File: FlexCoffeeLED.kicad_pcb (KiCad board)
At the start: 2 copper layers, 12.7 x 97.3 mm, 32 parts, among them IC1 NCP718ASN330T1G, IC2 PIC18F25K80-I_SO, IC3 MCP9904T-AE_9Q, J1 Conn_01x05_Male, J2 Conn_01x01_Male, J3 Conn_01x01_Male, Q1 2N3904, Q2 2N3904, Q3 2N3904, U1 PCA9306

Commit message: A Brand New Design
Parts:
- removed Q1, Q2, Q3: 2N3904, BillysCustomLibs:TO-92_Inline_Narrow_Oval_SMD
- removed R5: 450k, Resistors_SMD:R_0603
- removed R6: 200k, Resistors_SMD:R_0603
- removed R7, R8: 1k, Resistors_SMD:R_0603
- removed U1: PCA9306, SamacSys_Parts:SOP50P310X90-8N
- added C11: 0.1uF, Capacitors_SMD:C_0603, F.Cu at (195.6, 103.9)
- added IC4: LM75BDP,118, SamacSys_Parts:SOP65P490X110-8N, F.Cu at (187.6, 74.2)
- added LED4: WS2812B, LEDs:LED_WS2812B-PLCC4, F.Cu at (181.2, 57.9)
- added LED5: WS2812B, LEDs:LED_WS2812B-PLCC4, F.Cu at (181.2, 46.1)
- added LED6: WS2812B, LEDs:LED_WS2812B-PLCC4, F.Cu at (181.2, 34.3)
- C1, C4: value 1uF -> 15pF
- C7: value 2.2nF -> 15pF
- C8: value 2.2nF -> 0.1uF
- IC1: value NCP718ASN330T1G -> LM75BDP,118; footprint SamacSys_Parts:SOT95P280X100-5N -> SamacSys_Parts:SOP65P490X110-8N
- IC2: value PIC18F25K80-I_SO -> PIC16F18426-I_ST; footprint SamacSys_Parts:SOIC127P1030X265-28N -> SOP65P640X120-14N
- IC3: value MCP9904T-AE_9Q -> LM75BDP,118; footprint SamacSys_Parts:SON50P300X300X90-11N-D -> SamacSys_Parts:SOP65P490X110-8N
- J1: footprint BillysCustomLibs:Pin_Header_Straight_1x05_Pitch2.54mm_SMD_Flat -> Pin_Headers:Pin_Header_Straight_1x05_Pitch2.54mm
- J2, J3: value Conn_01x01_Male -> Conn_01x03_Male; footprint Pin_Headers:Pin_Header_Straight_1x01_Pitch2.54mm -> Pin_Headers:Pin_Header_Straight_1x03_Pitch2.54mm
- moved C7 66.2 mm to (173.5, 32.2), turned to 0 degrees
- moved JP1 64.3 mm to (168.1, 102.7)
- moved C2 64.2 mm to (170.4, 105.2)
- moved R2 64.2 mm to (168.7, 105.2)
- moved R1 63.6 mm to (168.7, 99.9)
- moved C8 61.8 mm to (196.9, 38.2), turned to 0 degrees
- moved IC3 60.5 mm to (187.7, 33.8)
- moved R3 56.3 mm to (195.7, 34.2)
- moved IC2 45.4 mm to (181.2, 97.7), turned to 270 degrees
- moved LED3 39.8 mm to (181.2, 69.7)
- moved C9 35.3 mm to (172.8, 101.4)
- moved C4 30.3 mm to (180.1, 70.9), turned to 180 degrees
- moved C6 22.5 mm to (180.5, 56.8), turned to 0 degrees
- moved C5 21.9 mm to (174.9, 93.8)
- moved C1 21.4 mm to (180.4, 86.5), turned to 180 degrees
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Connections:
- net Net-(IC2-Pad5) renamed /SCL2
- net Net-(IC2-Pad6) renamed /SDA2
- C1 pad 1: +5V -> /LED3
- C10 pad 1: /VREF2 -> +5V
- C2 pad 2: GND -> Net-(C2-Pad2)
- C3 pad 1: /LED1 -> /DIN
- C4 pad 1: +3V3 -> /LED4
- C6 pad 1: /LED3 -> /LED5
- C7 pad 1: /DP2 -> /LED6
- C7 pad 2: /DN2 -> GND
- C8 pad 1: /DP1 -> +5V
- C8 pad 2: /DN1 -> GND
- IC1 pad 1: +5V -> SDA_5V
- IC1 pad 2: GND -> SCL_5V
- IC1 pad 3: +5V -> Net-(IC1-Pad3)
- IC1 pad 5: +3V3 -> +5V
- IC2 pad 1: /MCLR -> +5V
- IC2 pad 10: Net-(IC2-Pad10) -> SCL_5V
- IC2 pad 11: Net-(IC2-Pad11) -> /DIN
- IC2 pad 12: Net-(IC2-Pad12) -> /PGC
- IC2 pad 13: Net-(IC2-Pad13) -> /PGD
- IC2 pad 14: SCL_5V -> GND
- IC2 pad 4: Net-(IC2-Pad4) -> /MCLR
- IC2 pad 8: GND -> Net-(IC2-Pad8)
- IC2 pad 9: Net-(IC2-Pad9) -> SDA_5V
- IC3 pad 1: +3V3 -> SDA_5V
- IC3 pad 2: /DP1 -> SCL_5V
- IC3 pad 3: /DN1 -> Net-(IC3-Pad3)
- IC3 pad 4: /DP2 -> GND
- IC3 pad 5: /DN2 -> +5V
- IC3 pad 6: GND -> Net-(IC3-Pad6)
- IC3 pad 7: Net-(IC3-Pad7) -> GND
- IC3 pad 8: Net-(IC3-Pad8) -> GND
- J2 pad 1: /LED1 -> /DIN
- J3 pad 1: /LED4 -> GND
- LED1 pad 4: /LED1 -> /DIN
- R3 pad 1: +3V3 -> +5V
- R3 pad 2: SDA_3V -> Net-(IC3-Pad6)
- R4 pad 1: +3V3 -> +5V
- R4 pad 2: SCL_3V -> Net-(IC4-Pad7)
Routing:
- net +5V: track 148.5 -> 0.00 mm, vias 16 -> 0
- net /LED1: track 79.5 -> 0.00 mm, vias 4 -> 0
- net /PGD: track 76.6 -> 0.00 mm, vias 2 -> 0
- net /DP1: track 76.4 -> 0.00 mm, vias 3 -> 0
- net /DN1: track 76.3 -> 0.00 mm, vias 2 -> 0
- net /PGC: track 75.7 -> 0.00 mm, vias 2 -> 0
- net /MCLR: track 74.7 -> 0.00 mm, vias 2 -> 0
- net /DP2: track 55.9 -> 0.00 mm, vias 4 -> 0
- net /DN2: track 48.2 -> 0.00 mm, vias 6 -> 0
- net /LED2: track 42.1 -> 0.00 mm, vias 2 -> 0
- net /LED3: track 37.6 -> 0.00 mm, vias 2 -> 0
- net SCL_5V: track 23.8 -> 0.00 mm
- net +3V3: track 22.3 -> 0.00 mm
- net SDA_5V: track 22.1 -> 0.00 mm
- net GND: track 15.0 -> 0.00 mm, vias 40 -> 0
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
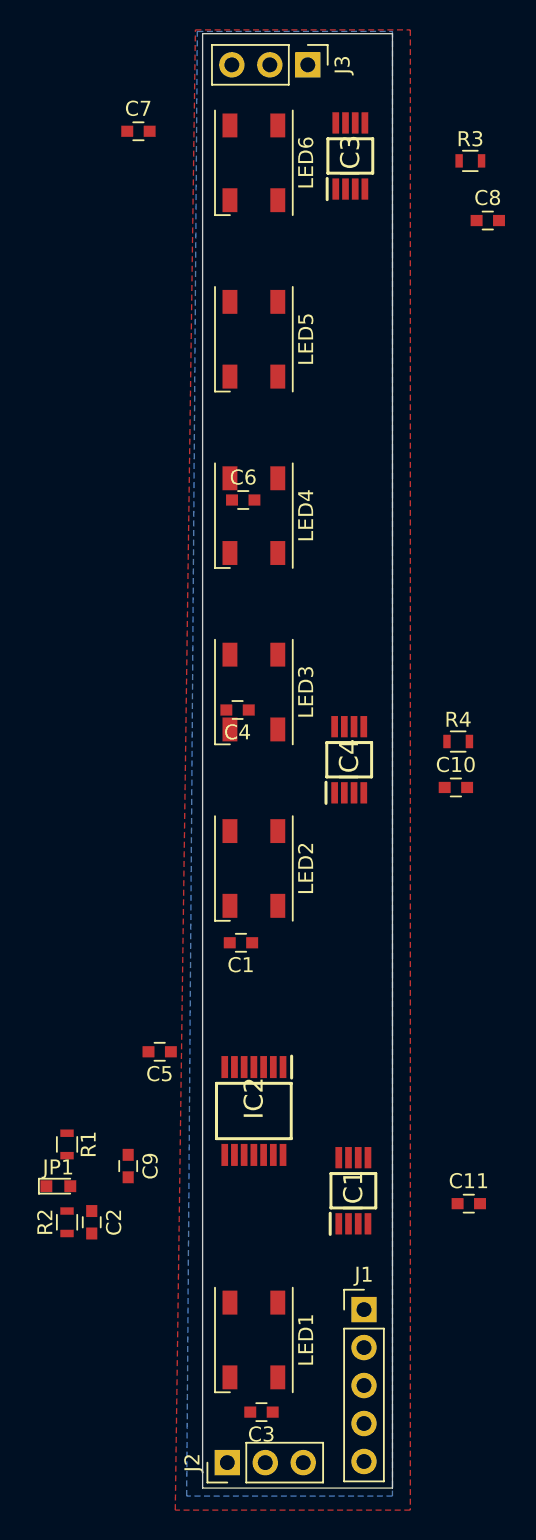
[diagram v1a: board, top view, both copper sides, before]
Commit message: Added .git attributes Routed New PCB Design Passed DRC.
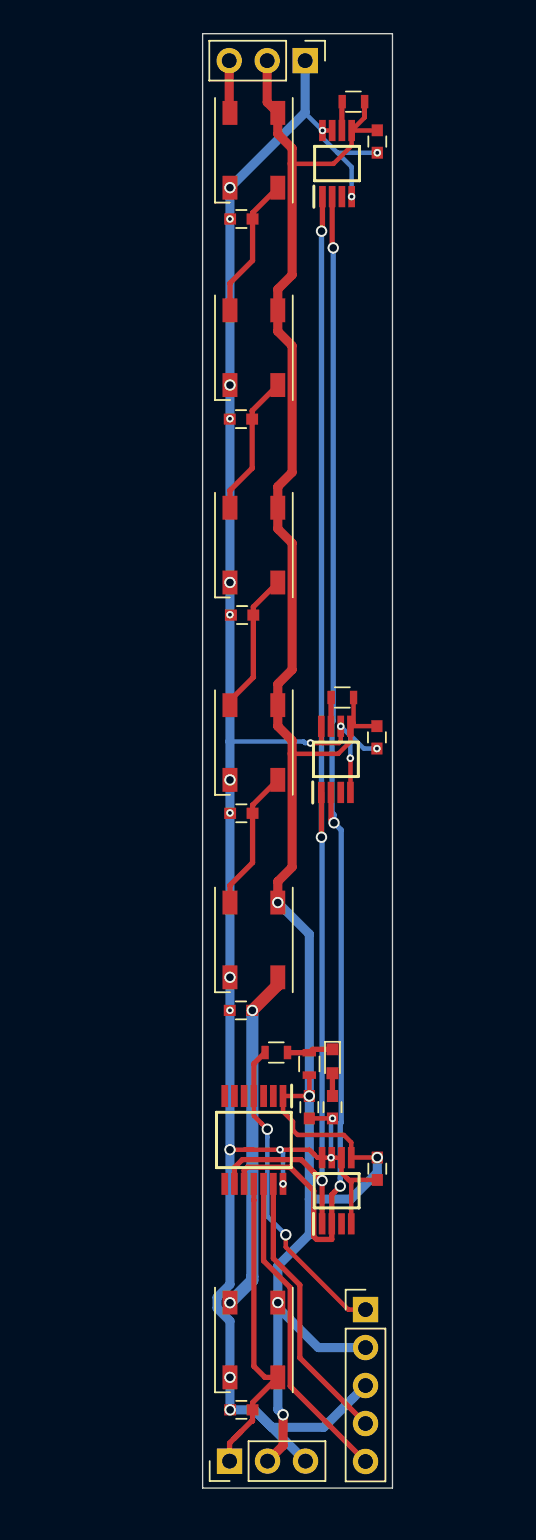
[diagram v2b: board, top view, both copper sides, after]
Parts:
- moved JP1 20.2 mm to (186.5, 94.4), turned to 270 degrees
- moved R2 18.0 mm to (182.7, 93.8), turned to 0 degrees
- moved C2 17.8 mm to (186.5, 97.5)
- moved R1 17.1 mm to (184.9, 94.6), turned to 90 degrees
- moved C9 12.7 mm to (184.9, 97.5)
- moved C8 9.09 mm to (189.5, 32.9), turned to 270 degrees
- moved C7 9.04 mm to (180.4, 38.0), turned to 180 degrees
- moved R3 8.77 mm to (187.9, 30.2), turned to 180 degrees
- moved C1 8.66 mm to (180.4, 77.8)
- moved R4 8.29 mm to (187.1, 70.1), turned to 180 degrees
- moved C11 6.55 mm to (189.5, 101.6), turned to 270 degrees
- moved C4 6.36 mm to (180.4, 64.5)
- moved C10 6.26 mm to (189.5, 72.7), turned to 270 degrees
- moved C5 6.10 mm to (180.4, 91.0)
- moved C6 5.41 mm to (180.4, 51.4), turned to 180 degrees
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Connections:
- C2 pad 2: Net-(C2-Pad2) -> GND
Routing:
- net GND: track 0.00 -> 157.5 mm, vias 0 -> 24
- net +5V: track 0.00 -> 145.4 mm, vias 0 -> 5
- net SCL_5V: track 0.00 -> 83.1 mm, vias 0 -> 3
- net SDA_5V: track 0.00 -> 80.0 mm, vias 0 -> 3
- net /LED2: track 0.00 -> 23.1 mm, vias 0 -> 2
- net /DIN: track 0.00 -> 21.7 mm
- net /PGC: track 0.00 -> 21.4 mm
- net /MCLR: track 0.00 -> 21.3 mm, vias 0 -> 2
- net /PGD: track 0.00 -> 18.6 mm
- net /LED4: track 0.00 -> 9.54 mm
- net /LED3: track 0.00 -> 9.53 mm
- net /LED6: track 0.00 -> 9.53 mm
- net /LED5: track 0.00 -> 9.53 mm
- net /DOUT: track 0.00 -> 3.52 mm
- net Net-(JP1-Pad1): track 0.00 -> 3.11 mm
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- removed copper zone on B.Cu, net GND
- removed copper zone on F.Cu, net GND
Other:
- rule via_min_drill: 0.3 -> 0.254

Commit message: Second Full Board Revision
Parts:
- moved J3 136.0 mm to (116.2, 144.9), turned to 0 degrees
- moved R3 131.1 mm to (118.9, 141.7), turned to 270 degrees
- moved LED6 129.2 mm to (122.2, 148.4), turned to 0 degrees
- moved C8 126.9 mm to (121.6, 140.1), turned to 0 degrees
- moved IC3 125.8 mm to (123.1, 142.8), turned to 180 degrees
- moved C7 123.4 mm to (126.8, 149.2), turned to 270 degrees
- moved LED5 111.6 mm to (135.4, 148.4), turned to 0 degrees
- moved C6 105.7 mm to (140.2, 149.2), turned to 270 degrees
- moved LED4 94.3 mm to (148.6, 148.4), turned to 0 degrees
- moved C4 88.9 mm to (153.3, 149.1), turned to 270 degrees
- moved LED3 77.8 mm to (161.8, 148.4), turned to 0 degrees
- moved R4 77.8 mm to (158.8, 142.4), turned to 270 degrees
- moved C10 73.0 mm to (161.4, 140.1), turned to 0 degrees
- moved C1 72.7 mm to (166.5, 149.2), turned to 270 degrees
- moved IC4 72.7 mm to (162.9, 142.9), turned to 180 degrees
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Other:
- board size 12.7 x 97.3 mm -> 97.3 x 12.7 mm
- board text added: "Coffee Cup Buddy Billy Bogardus 4/26/2019"
